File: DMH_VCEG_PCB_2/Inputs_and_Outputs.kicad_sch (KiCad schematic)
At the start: 7 parts, among them J1 TS_Jack_6.35mm_Sw, J2 TS_Jack_6.35mm_Sw, J200 IDC_02x05, J3 TS_Jack_6.35mm_Sw, J5 TS_Jack_6.35mm_Sw, J50 Conn_01x06, J60 Conn_01x06

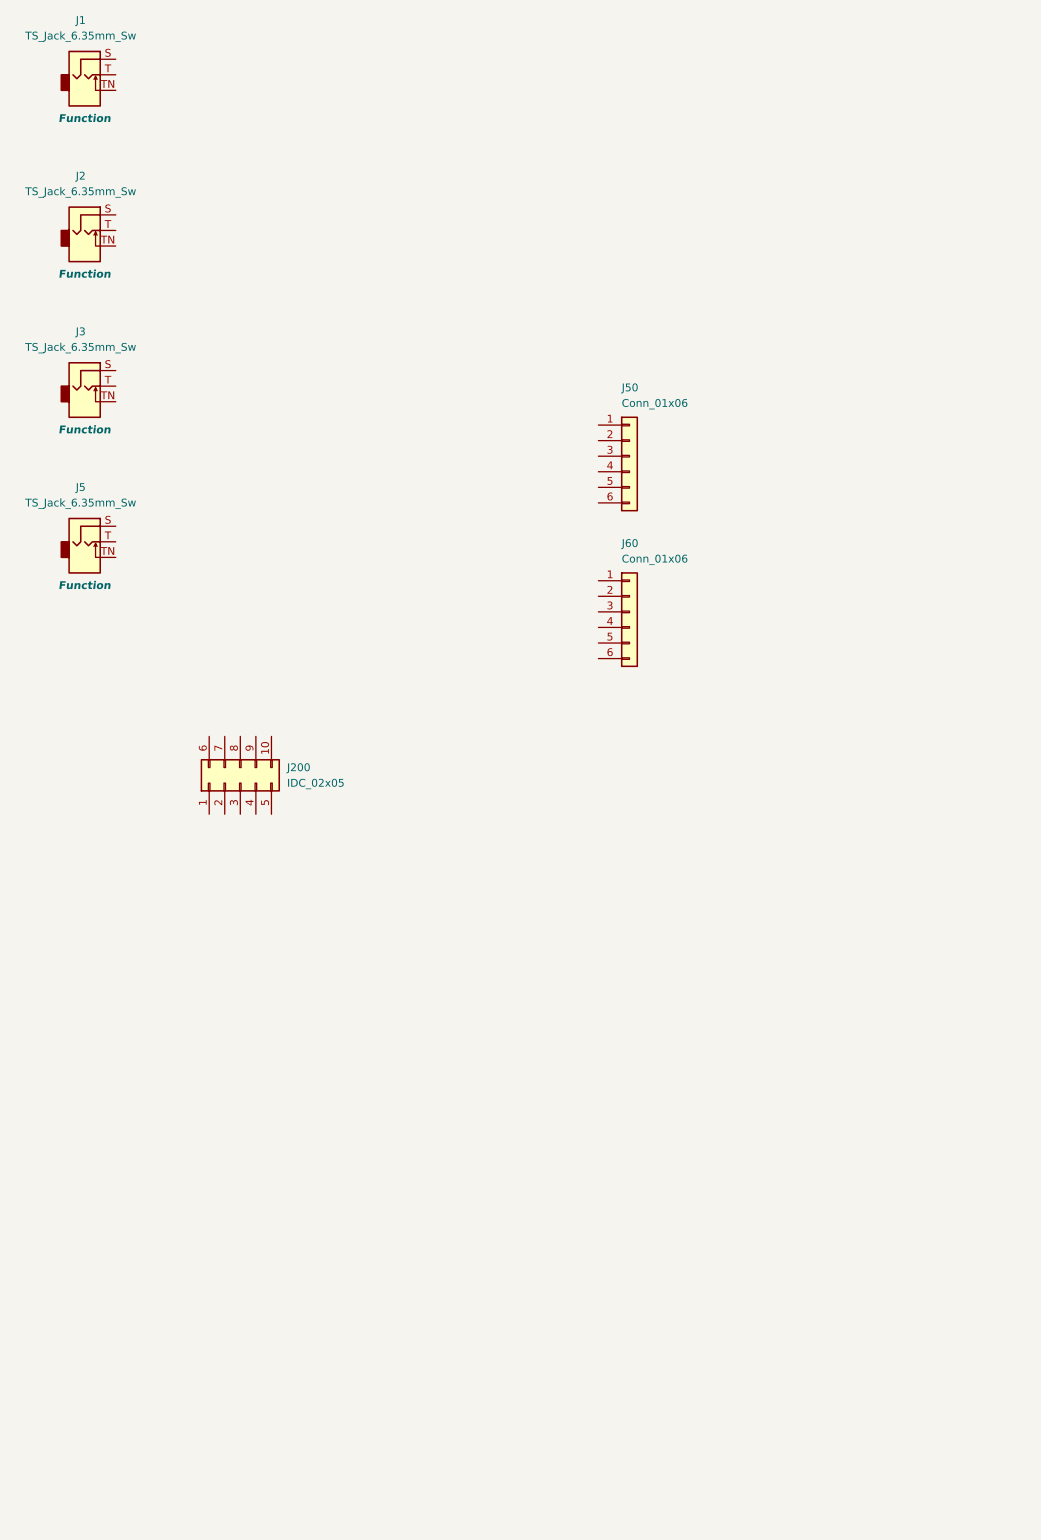
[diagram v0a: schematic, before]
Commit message: Copied PCB 1 as PCB 2
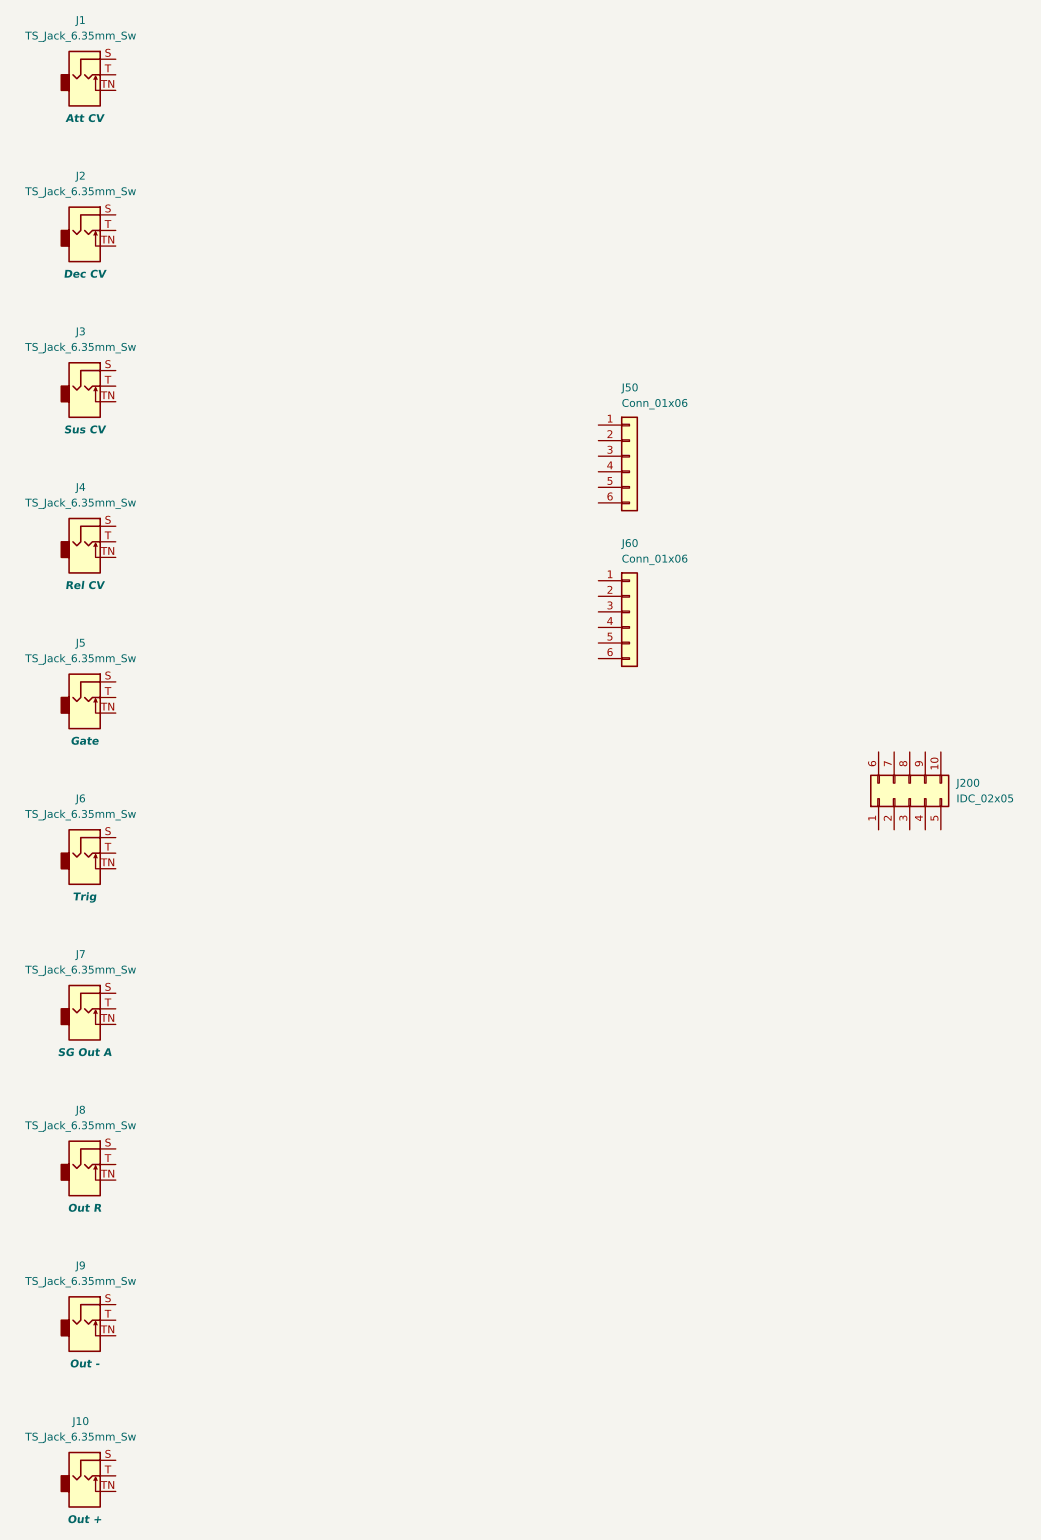
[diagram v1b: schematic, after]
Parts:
- added J10, J5, J6, J7, J8, J9: TS_Jack_6.35mm_Sw, SynthStuff:CUI_MJ-63052A, symbol SynthStuff:TS_Jack_6.35mm_Sw
- J1: Function Function -> Att CV
- J2: Function Function -> Dec CV
- J3: Function Function -> Sus CV
- J4: renamed from J5; Function Function -> Rel CV
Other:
- moved on the sheet: J200
